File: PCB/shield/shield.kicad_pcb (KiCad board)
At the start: 2 copper layers, 99.6 x 80.1 mm, 18 parts, among them J1 QTR-8A, J10 ESP32_left_m, J11 ESP32_right_m, J13 Conn_01x06, J14 Domino, J15 Domino, J2 QMC5883L, J3 Servo, J8 ESP32_left_f, J9 ESP32_right_f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

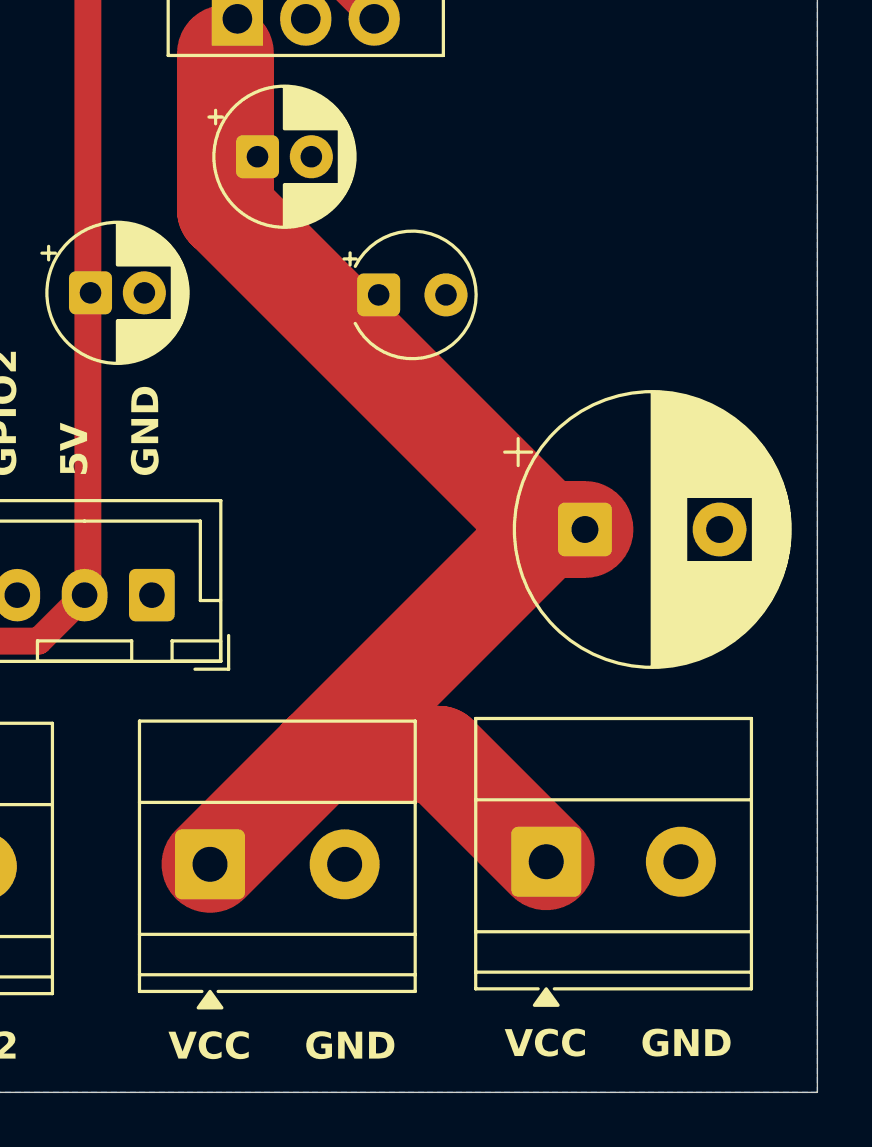
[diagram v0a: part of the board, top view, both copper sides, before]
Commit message: wip: adding reverse polar protection
Added 1N5822 to protect reverse polar
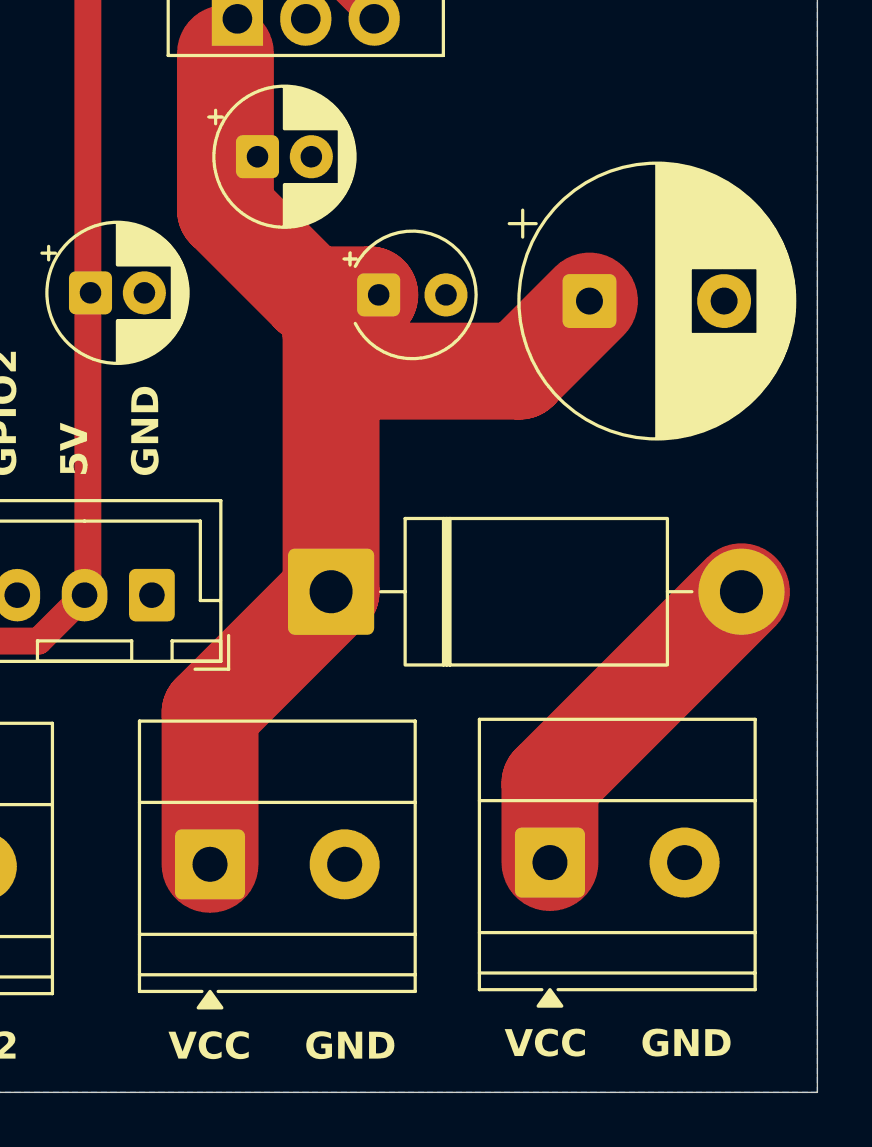
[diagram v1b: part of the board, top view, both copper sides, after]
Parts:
- removed the J15 at (177.1, 138.5)
- added D1: 1N5822, Diode_THT:D_DO-201AD_P15.24mm_Horizontal, F.Cu at (169.1, 128.5)
- added J4: Domino, TerminalBlock_Phoenix:TerminalBlock_Phoenix_MKDS-1,5-2_1x02_P5.00mm_Horizontal, F.Cu at (177.2, 138.5)
- moved C1 8.49 mm to (178.7, 117.7)
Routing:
- net Net-(D1-A): track 0.00 -> 13.0 mm
- net VCC: track 51.7 -> 47.3 mm

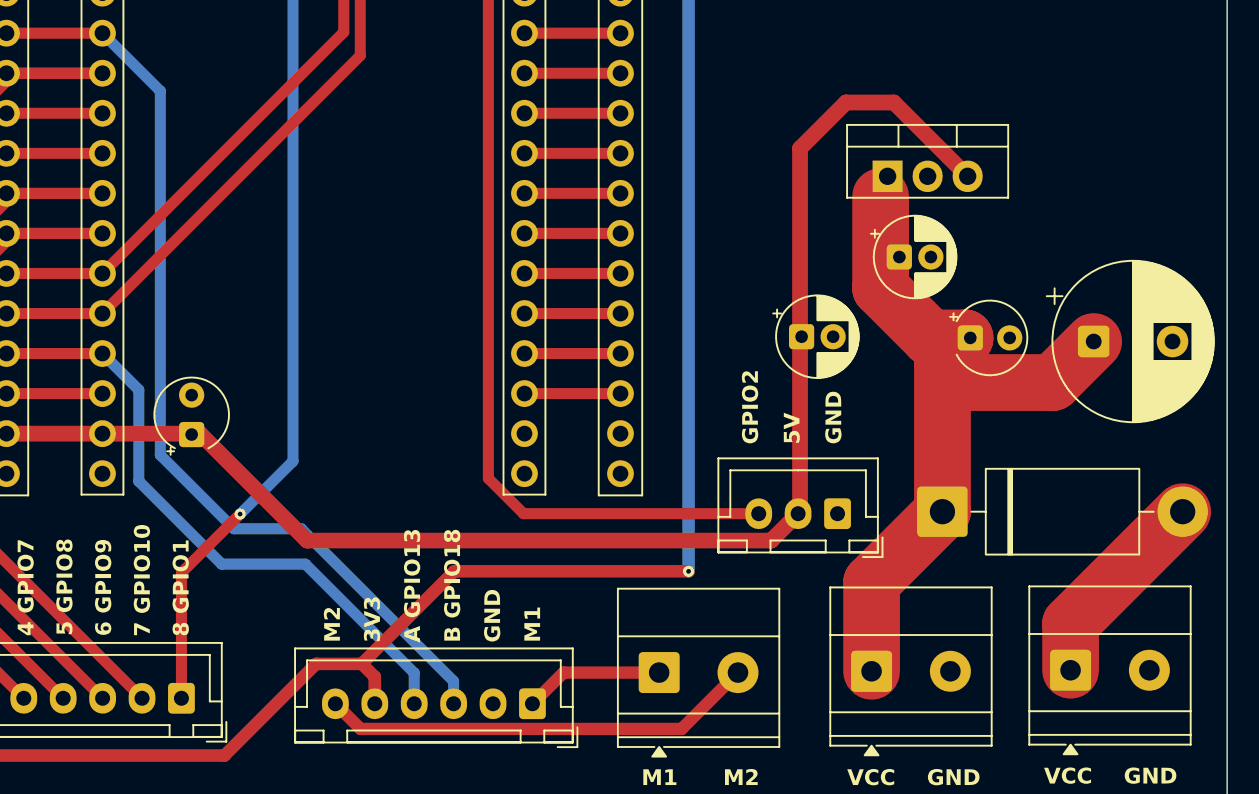
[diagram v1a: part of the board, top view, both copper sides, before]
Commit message: feat: change THT to SMD
Changed LM7805 to AMS1117
Changed THT capacitor to SMD capacitor
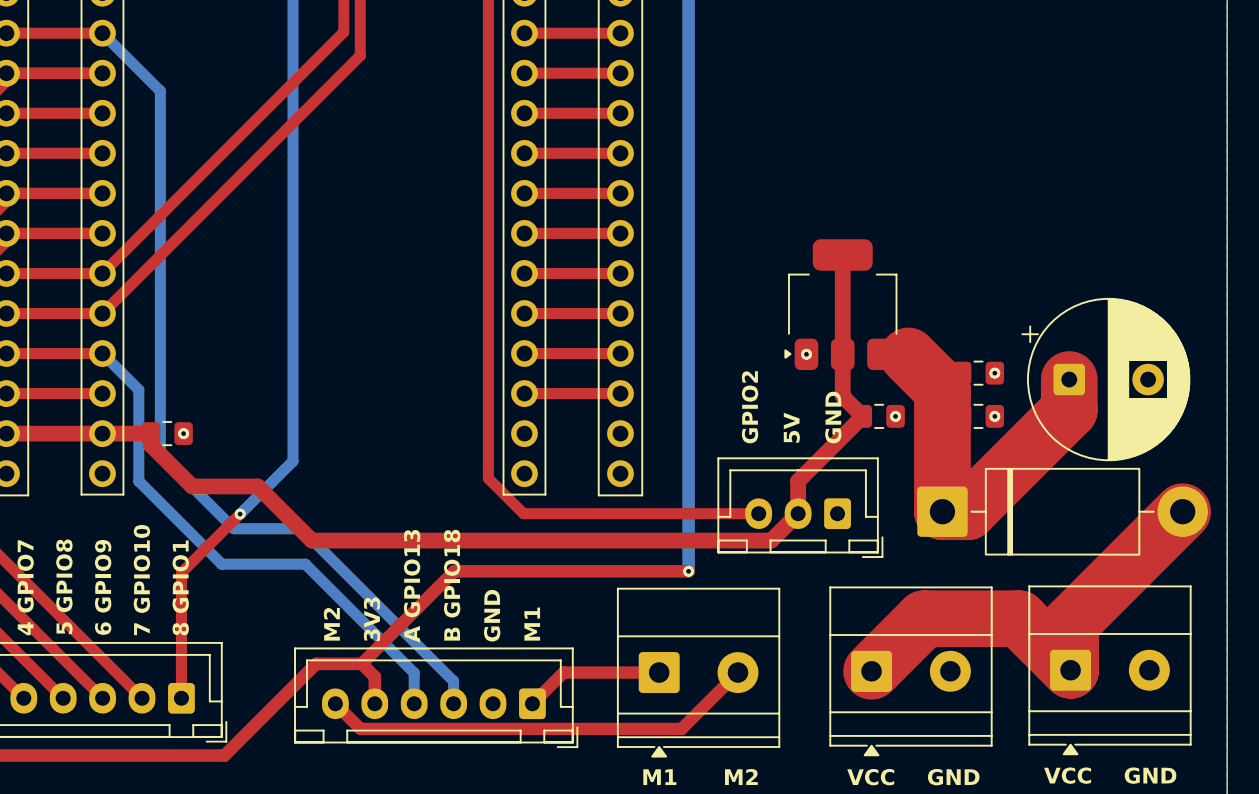
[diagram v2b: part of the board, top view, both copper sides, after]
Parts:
- removed U1: L7805, Package_TO_SOT_THT:TO-220-3_Vertical
- added U2: AMS1117, Package_TO_SOT_SMD:SOT-223-3_TabPin2, F.Cu at (162.8, 115.3)
- C2, C4: footprint Capacitor_THT:CP_Radial_D5.0mm_P2.00mm -> Capacitor_SMD:C_0805_2012Metric_Pad1.18x1.45mm_HandSolder
- C3, C5: footprint Capacitor_THT:CP_Radial_Tantal_D4.5mm_P2.50mm -> Capacitor_SMD:C_0805_2012Metric_Pad1.18x1.45mm_HandSolder
- moved C2 8.91 mm to (171.4, 119.7)
- moved C4 7.05 mm to (165.1, 122.4)
- moved C3 5.01 mm to (171.4, 122.4)
- moved C1 2.87 mm to (177.1, 120.1)
- moved C5 1.55 mm to (119.9, 123.5), turned to 0 degrees
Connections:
- J15 pad 1: VCC -> Net-(D1-A)
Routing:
- net VCC: track 47.3 -> 23.4 mm
- net +5V: track 90.6 -> 72.8 mm
- net Net-(D1-A): track 13.0 -> 28.4 mm
- net GND: vias 0 -> 5

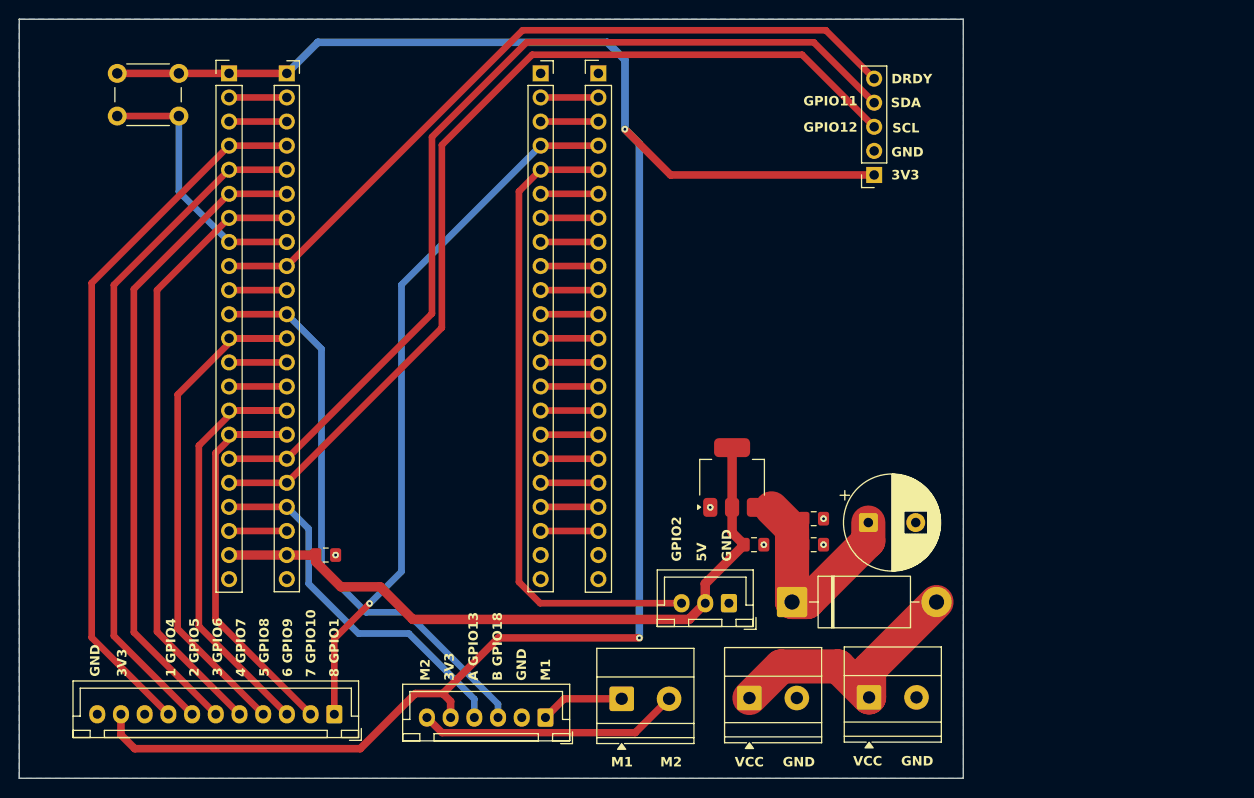
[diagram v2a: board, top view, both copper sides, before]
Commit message: feat: added socket for joystick module
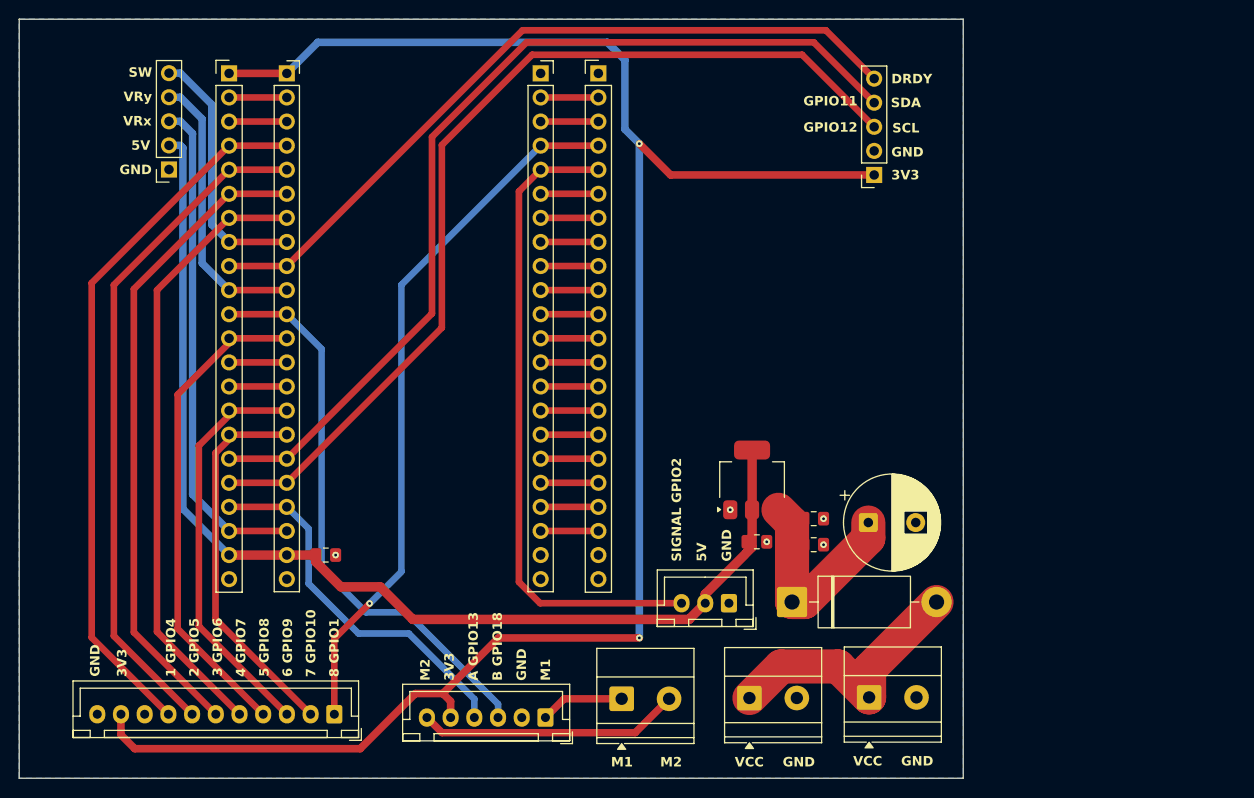
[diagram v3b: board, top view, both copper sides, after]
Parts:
- removed SW1: SW_Push, Button_Switch_THT:SW_PUSH_6mm_H5mm
- added J5: Joystick, Connector_PinSocket_2.54mm:PinSocket_1x05_P2.54mm_Vertical, F.Cu at (103.4, 82.9)
- moved U2 2.12 mm to (164.9, 115.6)
- moved C4 0.43 mm to (165.4, 122.1)
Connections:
- net /M1 renamed Net-(J13-Pin_1)
- net /M2 renamed Net-(J13-Pin_6)
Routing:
- net +5V: track 72.8 -> 118.7 mm
- net /GPIO14: track 12.2 -> 52.6 mm
- net /GPIO17: track 12.2 -> 29.8 mm
- net +3V3: track 210.7 -> 196.8 mm
- net /GPIO10: track 52.2 -> 40.5 mm
- net /GPIO9: track 55.2 -> 43.5 mm
- net /GPIO8: track 63.6 -> 51.9 mm
- net /GPIO15: track 34.2 -> 27.2 mm
- net Net-(J10-Pin_3): track 12.2 -> 6.09 mm
- net Net-(J10-Pin_2): track 12.2 -> 6.09 mm
- net Net-(J10-Pin_14): track 12.2 -> 6.09 mm
- net Net-(J10-Pin_13): track 12.2 -> 6.09 mm
- net /GPIO7: track 71.3 -> 65.2 mm
- net /GPIO6: track 74.8 -> 68.7 mm
- net /GPIO5: track 78.1 -> 72.0 mm
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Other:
- board text added: "SIGNAL GPIO2"
- board text added: "SW"
- board text added: "VRx"
- board text added: "VRy"
- board text removed: "GPIO2"

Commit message: feat: add lcd oled screen socket
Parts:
- added J6: OLED, Connector_PinSocket_2.54mm:PinSocket_1x04_P2.54mm_Vertical, F.Cu at (157.9, 102.9)
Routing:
- net /GPIO12+SCL: track 101.2 -> 129.1 mm
- net /GPIO11+SDA: track 99.8 -> 127.7 mm
- net +5V: track 118.7 -> 134.3 mm
